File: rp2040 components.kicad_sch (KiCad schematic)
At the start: 29 parts, among them J1 SWD, SW27 SW_Push, U2 W25Q128JVS, U3 XC6206PxxxMR, U4 USBLC6-2SC6, Y1 12MHz

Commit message: added reset button
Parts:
- added SW38: SW_Push, Keebio-Parts:SW_SPST_TL3342, symbol Switch:SW_Push
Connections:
- net GND: now also SW38.2
- net RESET: now also SW38.1
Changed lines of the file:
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@@
+    )
+  )
+  (global_label "RESET" (shape input) (at 81.915 113.03 180) (fields_autoplaced)
+    (effects (font (size 1.27 1.27)) (justify right))
+    (property "Intersheet References" "${INTERSHEET_REFS}" (id 0) (at 73.7567 112.9506 0)
+      (effects (font (size 1.27 1.27)) (justify right) hide)
     )
   )
@@
     )
     (property "Datasheet" "~" (id 3) (at 239.649 80.01 0)
+      (effects (font (size 1.27 1.27)) hide)
+    )
+    (pin "1")
+    (pin "2")
+  )
+  (symbol (lib_id "Switch:SW_Push") (at 86.995 113.03 0) (unit 1)
+    (in_bom yes) (on_board yes) (fields_autoplaced)
+    (property "Reference" "SW38" (id 0) (at 86.995 104.648 0))
+    (property "Value" "SW_Push" (id 1) (at 86.995 107.188 0))
+    (property "Footprint" "Keebio-Parts:SW_SPST_TL3342" (id 2) (at 86.995 107.95 0)
+      (effects (font (size 1.27 1.27)) hide)
+    )
+    (property "Datasheet" "~" (id 3) (at 86.995 107.95 0)
       (effects (font (size 1.27 1.27)) hide)
     )
@@
       (effects (font (size 1.27 1.27)) hide)
     )
+    (pin "1")
+  )
+  (symbol (lib_id "power:GND") (at 92.075 113.03 0) (unit 1)
+    (in_bom yes) (on_board yes) (fields_autoplaced)
+    (property "Reference" "#PWR0148" (id 0) (at 92.075 119.38 0)
+      (effects (font (size 1.27 1.27)) hide)
+    )
+    (property "Value" "GND" (id 1) (at 92.075 118.618 0))
+    (property "Footprint" "" (id 2) (at 92.075 113.03 0)
+      (effects (font (size 1.27 1.27)) hide)
+    )
+    (property "Datasheet" "" (id 3) (at 92.075 113.03 0)
+      (effects (font (size 1.27 1.27)) hide)
+    )

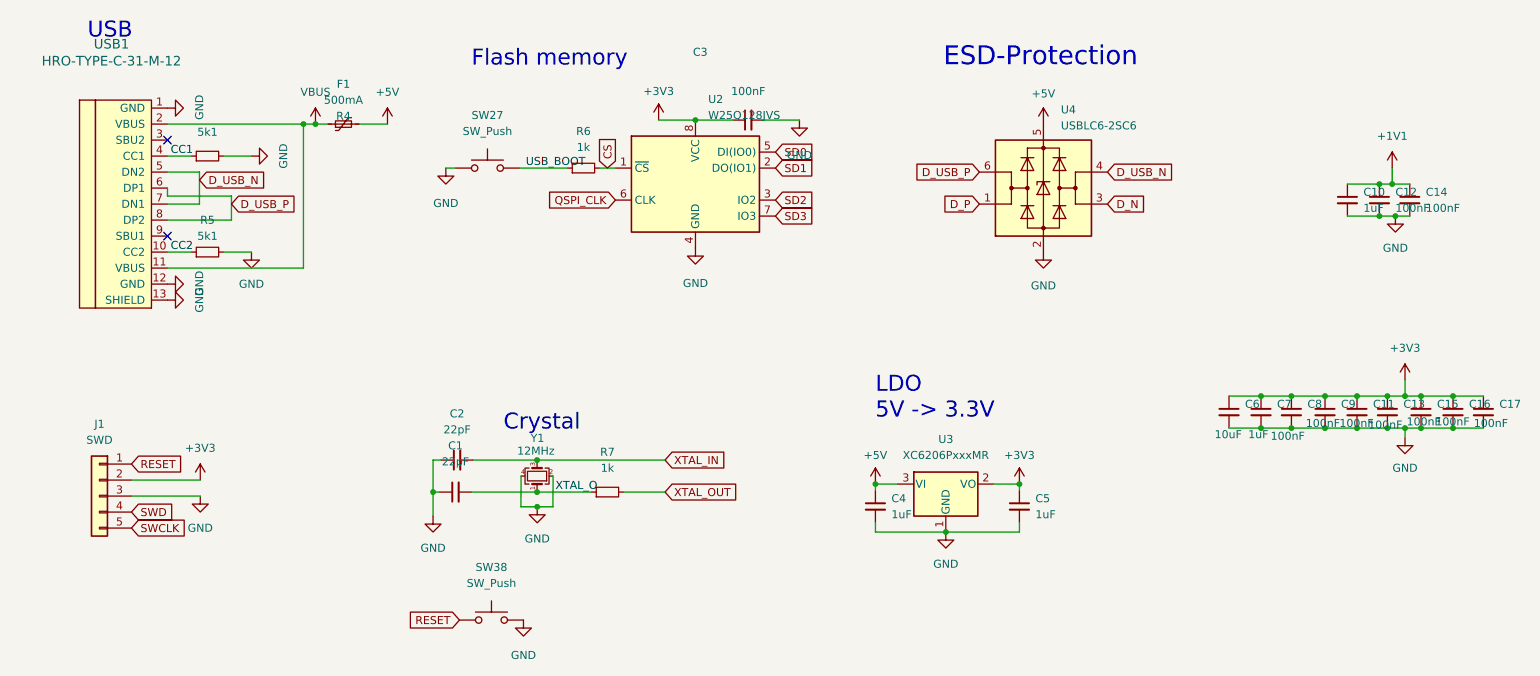
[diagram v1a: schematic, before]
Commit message: labelling of KLE options
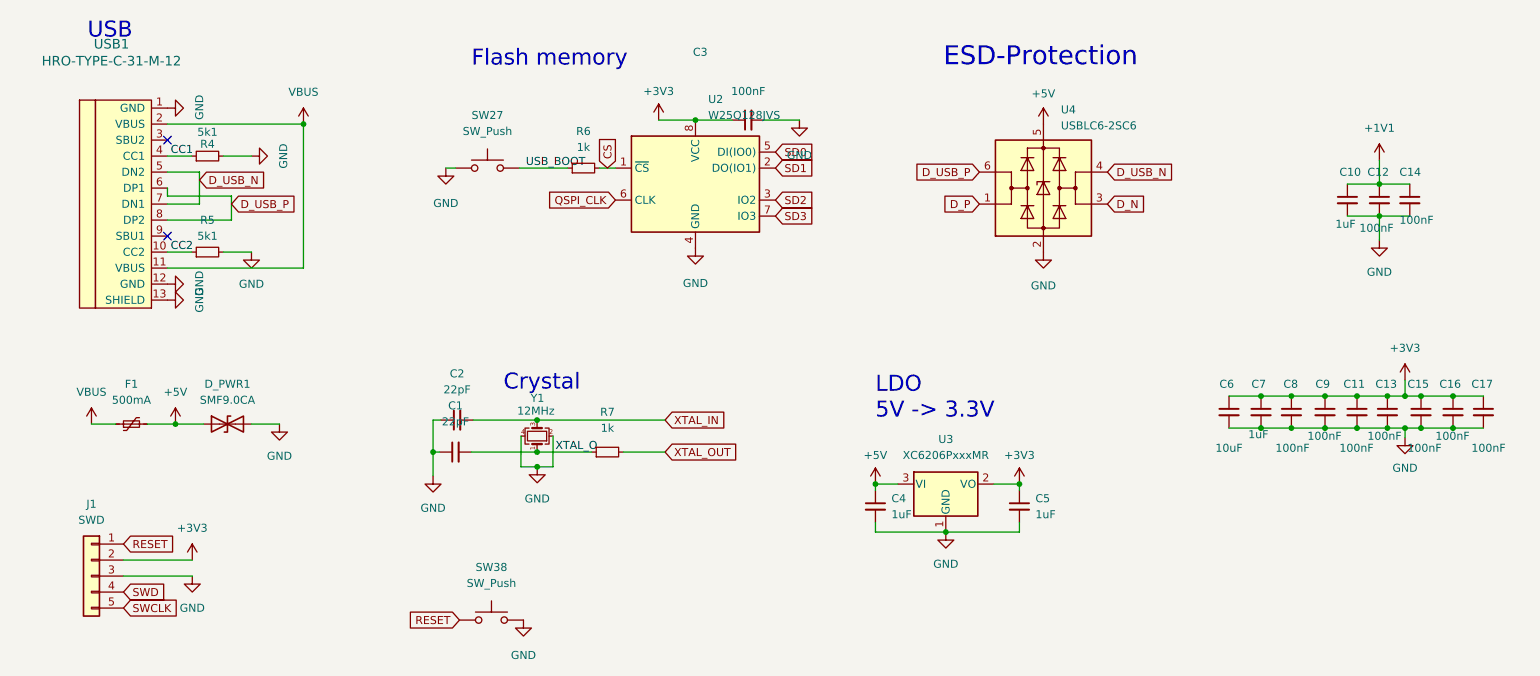
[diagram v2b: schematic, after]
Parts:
- added D_PWR1: SMF9.0CA, Diode_SMD:D_SOD-123, symbol Device:D_TVS
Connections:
- net +5V: now also D_PWR1.1 (A1)
- net GND: now also D_PWR1.2 (A2)
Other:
- moved on the sheet: C1, C2, F1, J1, R7, Y1
